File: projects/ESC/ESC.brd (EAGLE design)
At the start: 139.7 x 38.1 mm, 91 parts, among them J1 1755529, J2 1755529, J3 1755529, J4 1755529, U1 STM32F405RGT6, U10 CSD88584Q5DCT, U11 CSD88584Q5DCT, U12 CSD88584Q5DCT, U13 CSD88584Q5DCT, U2 CSD88584Q5DCT, U3 CSD88584Q5DCT, U4 CSD88584Q5DCT, U5 CSD88584Q5DCT, U6 CSD88584Q5DCT, U7 CSD88584Q5DCT, U8 CSD88584Q5DCT, U9 CSD88584Q5DCT, Y1 ECS-80-S-4X

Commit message: RIPUP MY LIFE
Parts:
- removed U$7: SAMTEC, VESC_SHIT:SAMTEC
- U$5: value SAMTEC -> ESC2BACKPLANE; device VESC_SHIT:SAMTEC -> ESC_to_Backplane_Connectors:ESC2BACKPLANE_WHOLE
- moved RED_LED 44.3 mm to (53.3, 6.10), turned to 90 degrees
- moved GREEN_LED 43.4 mm to (55.1, 6.10), turned to 90 degrees
- moved R2 40.1 mm to (53.3, 9.40), turned to 90 degrees
- moved R1 39.1 mm to (55.1, 9.40), turned to 90 degrees
- moved U3 38.9 mm to (21.6, 71.9)
- moved C13 38.9 mm to (43.9, 67.8)
- moved C14 38.9 mm to (38.1, 57.7)
- moved C17 38.9 mm to (41.9, 67.8)
- moved C22 38.9 mm to (35.4, 43.8)
- moved C23 38.9 mm to (33.7, 44.6)
- moved C24 38.9 mm to (43.9, 44.1)
- moved C25 38.9 mm to (44.1, 49.1)
- moved R10 38.9 mm to (43.7, 56.9)
- moved R11 38.9 mm to (46.0, 56.9)
- moved R18 38.9 mm to (30.1, 50.9)
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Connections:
- removed net 12V: U$5.P1-1, U$5.P1-2, U$5.P1-3, U$5.P1-4, U$5.P1-5, U$5.P1-6, U$5.P1-7, U$5.P1-8, U$5.P2-1, U$5.P2-2, U$5.P2-3, U$5.P2-4, U$5.P2-5, U$5.P2-6, U$5.P2-7, U$5.P2-8, U$5.P3-1, U$5.P3-2, U$5.P3-3, U$5.P3-4, U$5.P3-5, U$5.P3-6, U$5.P3-7, U$5.P3-8, U$5.P4-1, U$5.P4-2, U$5.P4-3, U$5.P4-4, U$5.P4-5, U$5.P4-6, U$5.P4-7, U$5.P4-8
- net +3V3: no longer U$5.1, U$5.10, U$5.11, U$5.12, U$5.13, U$5.14, U$5.15, U$5.16, U$5.17, U$5.18, U$5.19, U$5.2, U$5.20, U$5.21, U$5.22, U$5.23, U$5.24, U$5.3, U$5.4, U$5.5, U$5.6, U$5.7, U$5.8, U$5.9
- net CAN_H: no longer U$7.24
- net CAN_L: no longer U$7.23
- net GND: no longer U$7.P1-1, U$7.P1-2, U$7.P1-3, U$7.P1-4, U$7.P1-5, U$7.P1-6, U$7.P1-7, U$7.P1-8, U$7.P2-1, U$7.P2-2, U$7.P2-3, U$7.P2-4, U$7.P2-5, U$7.P2-6, U$7.P2-7, U$7.P2-8, U$7.P3-1, U$7.P3-2, U$7.P3-3, U$7.P3-4, U$7.P3-5, U$7.P3-6, U$7.P3-7, U$7.P3-8, U$7.P4-1, U$7.P4-2, U$7.P4-3, U$7.P4-4, U$7.P4-5, U$7.P4-6, U$7.P4-7, U$7.P4-8
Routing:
- net +3V3: track 144.9 -> 47.8 mm
- net VM_2: track 70.8 -> 0.00 mm, vias 6 -> 0
- net VM_1: track 64.5 -> 0.00 mm, vias 4 -> 0
- net NRST: track 85.5 -> 24.6 mm
- net INHC_3: track 69.9 -> 16.1 mm
- net INL_3: track 73.5 -> 21.0 mm
- net INHB_3: track 66.2 -> 18.3 mm
- net INHA_3: track 65.8 -> 18.9 mm
- net EN_3: track 60.1 -> 19.1 mm
- net FAULT_3: track 66.8 -> 25.9 mm
- net SWDIO: track 40.5 -> 1.78 mm
- net INHC_4: track 56.9 -> 20.0 mm
- net SLA_2: track 36.0 -> 0.00 mm
- net SWCLK: track 37.1 -> 1.87 mm
- net INL_4: track 59.1 -> 24.4 mm
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- removed copper zone on layer 1, net +3V3
- removed copper zone on layer 1, net 12V
- removed copper zone on layer 1, net 12V1

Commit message: Some changes have been made
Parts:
- moved U5 47.4 mm to (13.8, 10.4)
- moved U6 40.1 mm to (13.8, 4.06)
- moved U7 34.2 mm to (13.8, 17.0)

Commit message: making some changes
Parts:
- added C6: 0.1uF, SparkFun-Capacitors:0603
- added R6: 1.5k, SparkFun-Resistors:0603
- added U14: SN74CBTLV3257PWR, SN74CBTLV3257PWR:SN74CBTLV3257PWR
- moved U$5 44.1 mm to (53.3, 35.8), turned to 270 degrees
- moved GREEN_LED 3.84 mm to (58.9, 5.59)
- moved RED_LED 3.84 mm to (57.1, 5.59)
- moved R1 3.84 mm to (58.9, 8.89)
- moved R2 3.84 mm to (57.1, 8.89)
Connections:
- new net +12V: U$5.P$10, U$5.P$11, U$5.P$12, U$5.P$13, U$5.P$23, U$5.P$24, U$5.P$25, U$5.P$26, U$5.P$27, U$5.P$9, U$5.P$A, U$5.P$B, U$5.P$C, U$5.P$D, U$5.P$E, U$5.P$O, U$5.P$P, U$5.P$Q, U$5.P$R, U$5.P$S
- new net N$10: R6.1, U14.P$15
- new net NRST_IN: U14.P$9
- new net PROG_SEL: U$5.P$5
- new net S: U$6.S, U14.P$1
- new net SWCLK_IN: U14.P$4
- new net SWDIO_IN: U14.P$7
- net +3V3: now also C6.1, R6.2, U$5.P$G, U$5.P$H, U$5.P$U, U$5.P$V, U14.P$16
- net CAN_H: now also U$5.P$6
- net CAN_L: now also U$5.P$7
- net GND: now also C6.2, U$5.P$1, U$5.P$15, U$5.P$16, U$5.P$17, U$5.P$18, U$5.P$2, U$5.P$3, U$5.P$4, U$5.P$AA, U$5.P$BB, U$5.P$J, U$5.P$K, U$5.P$L, U$5.P$M, U$5.P$N, U$5.P$X, U$5.P$Y, U$5.P$Z, U14.P$8
- net NRST: now also U14.P$11
- net SWCLK: now also U14.P$2
- net SWDIO: now also U14.P$5
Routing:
- net FAULT_3: track 25.9 -> 2.42 mm, vias 1 -> 0
- net INL_4: track 24.4 -> 2.97 mm, vias 1 -> 0
- net GLC_3: track 21.1 -> 0.00 mm, vias 2 -> 0
- net SLC_3: track 24.1 -> 3.57 mm, vias 2 -> 0
- net NRST: track 24.6 -> 4.51 mm, vias 3 -> 1
- net EN_4: track 20.1 -> 0.03 mm
- net INL_3: track 21.0 -> 2.25 mm, vias 1 -> 0
- net INHC_4: track 20.0 -> 1.46 mm, vias 1 -> 0
- net VM_3: track 84.2 -> 66.3 mm, vias 2 -> 0
- net FAULT_4: track 17.8 -> 0.04 mm
- net SLB_3: track 20.0 -> 2.97 mm, vias 2 -> 1
- net INHB_4: track 19.4 -> 2.69 mm, vias 1 -> 0
- net EN_3: track 19.1 -> 2.50 mm, vias 1 -> 0
- net SHA_4: track 16.5 -> 0.54 mm
- net INHA_4: track 18.0 -> 2.23 mm, vias 1 -> 0
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- removed copper zone on layer 1, net VM_4

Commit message: REDESIGN preliminary 1
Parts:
- moved U3 43.7 mm to (13.5, 29.0)
- moved U4 40.2 mm to (23.1, 29.0), turned to 270 degrees
- moved U2 37.2 mm to (33.3, 29.0)
- moved C14 36.0 mm to (47.2, 22.9), flipped to the top, turned to 270 degrees
- moved C15 35.8 mm to (40.4, 35.6), turned to 180 degrees
- moved R7 35.8 mm to (41.5, 22.7), turned to 90 degrees
- moved C13 35.2 mm to (47.5, 32.8), turned to 0 degrees
- moved R8 34.2 mm to (42.6, 22.8), flipped to the bottom, turned to 180 degrees
- moved R11 34.2 mm to (48.8, 22.9), flipped to the bottom, turned to 0 degrees
- moved U$2 34.2 mm to (43.4, 28.7)
- moved R10 34.1 mm to (45.7, 22.9), flipped to the bottom, turned to 0 degrees
- moved R9 33.3 mm to (39.6, 22.9), turned to 180 degrees
- moved C17 32.4 mm to (44.7, 35.6), turned to 180 degrees
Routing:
- net SLA_1: track 0.00 -> 40.3 mm, vias 0 -> 2
- net GLA_1: track 0.00 -> 37.4 mm, vias 0 -> 2
- net SHA_1: track 0.00 -> 36.7 mm, vias 0 -> 2
- net GHA_1: track 0.00 -> 32.8 mm, vias 0 -> 2
- net PHASE_C1: track 0.00 -> 31.8 mm
- net SLB_1: track 0.00 -> 29.3 mm, vias 0 -> 2
- net SHB_1: track 0.00 -> 23.2 mm, vias 0 -> 2
- net PHASE_B1: track 0.00 -> 23.0 mm
- net GHB_1: track 0.00 -> 21.2 mm, vias 0 -> 2
- net GLB_1: track 0.00 -> 20.8 mm, vias 0 -> 2
- net PHASE_A1: track 0.00 -> 18.2 mm
- net SLC_1: track 0.00 -> 11.5 mm
- net SHC_1: track 0.00 -> 11.4 mm
- net N$19: track 0.00 -> 10.4 mm, vias 0 -> 1
- net GHC_1: track 0.00 -> 8.71 mm, vias 0 -> 2
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- added copper zone on layer 1, net VM_1

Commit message: some stuff
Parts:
- moved U$1 43.8 mm to (42.5, 6.96)
- moved U7 10.5 mm to (22.2, 10.7)
- moved U5 5.34 mm to (14.1, 15.7)
- moved U6 0.80 mm to (14.1, 4.83)

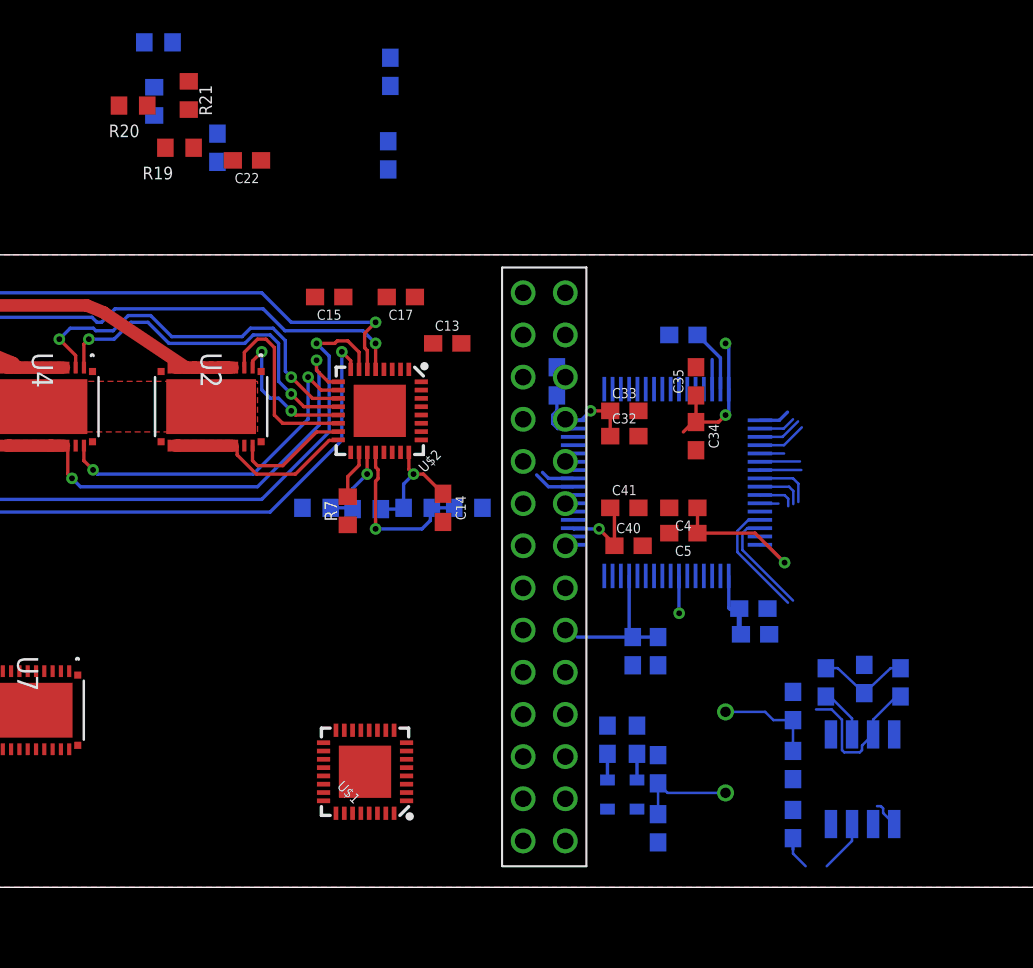
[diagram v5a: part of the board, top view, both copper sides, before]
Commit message: continued edits of drv setup
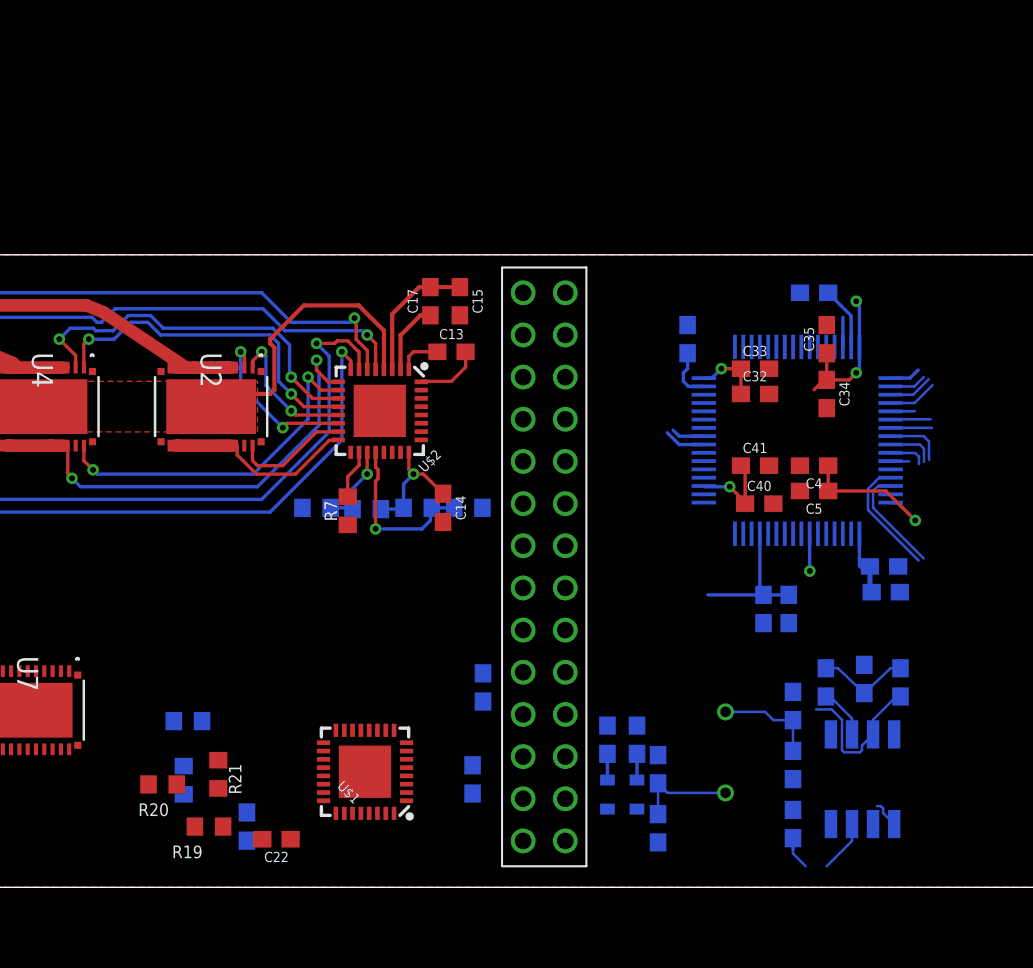
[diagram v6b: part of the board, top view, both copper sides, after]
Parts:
- moved R18 40.9 mm to (31.9, 10.0)
- moved C22 40.9 mm to (37.2, 2.90)
- moved C23 40.9 mm to (35.4, 3.66)
- moved R19 40.9 mm to (33.1, 3.66)
- moved R20 40.9 mm to (30.4, 6.20)
- moved R21 40.9 mm to (33.7, 6.81)
- moved R22 40.9 mm to (31.6, 6.45)
- moved C24 37.9 mm to (49.0, 6.50)
- moved C25 37.5 mm to (49.7, 12.0)
- moved C32 8.27 mm to (66.0, 29.7)
- moved C33 8.27 mm to (66.0, 31.2)
- moved C41 8.27 mm to (66.0, 25.4)
- moved C1 8.27 mm to (69.6, 35.8)
- moved C16 8.27 mm to (68.1, 16.8)
- moved C3 8.27 mm to (62.0, 33.0)
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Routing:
- net VM_1: track 0.00 -> 26.1 mm
- net N$34: track 0.00 -> 4.35 mm
- net N$16: track 0.00 -> 3.96 mm
- net N$9: track 0.00 -> 2.61 mm
- net SHC_1: track 11.4 -> 10.1 mm, vias 0 -> 2
- net SHA_1: track 36.7 -> 35.7 mm

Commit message: other edits
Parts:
- moved C6 83.5 mm to (80.5, 10.9), turned to 90 degrees
- moved R6 81.6 mm to (80.5, 14.2), turned to 90 degrees
- moved U14 68.9 mm to (67.6, 15.0)
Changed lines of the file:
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@@
 <attribute name="VALUE" x="68.64743125" y="13.90911875" size="1.27245" layer="28" rot="MR270"/>
 </element>
-<element name="U14" library="SN74CBTLV3257PWR" package="SN74CBTLV3257PWR" value="SN74CBTLV3257PWR" x="1.016" y="-3.048" smashed="yes">
-<attribute name="NAME" x="2.286" y="-14.478" size="1.016" layer="25" ratio="7"/>
-<attribute name="VALUE" x="2.286" y="-1.778" size="1.016" layer="25" ratio="7"/>
+<element name="U14" library="SN74CBTLV3257PWR" package="SN74CBTLV3257PWR" value="SN74CBTLV3257PWR" x="67.564" y="14.986" smashed="yes">
+<attribute name="NAME" x="68.834" y="3.556" size="1.016" layer="25" ratio="7"/>
+<attribute name="VALUE" x="68.834" y="16.256" size="1.016" layer="25" ratio="7"/>
 </element>
-<element name="C6" library="SparkFun-Capacitors" library_urn="urn:adsk.eagle:library:510" package="0603" package3d_urn="urn:adsk.eagle:package:37414/1" value="0.1uF" x="1.778" y="-16.764" smashed="yes">
-<attribute name="NAME" x="1.778" y="-16.002" size="0.6096" layer="25" font="vector" ratio="20" align="bottom-center"/>
-<attribute name="PROD_ID" value="CAP-00810" x="-6.604" y="-1.778" size="1.778" layer="27" display="off"/>
-<attribute name="VALUE" x="1.778" y="-17.526" size="0.6096" layer="27" font="vector" ratio="20" align="top-center"/>
+<element name="C6" library="SparkFun-Capacitors" library_urn="urn:adsk.eagle:library:510" package="0603" package3d_urn="urn:adsk.eagle:package:37414/1" value="0.1uF" x="80.518" y="10.922" smashed="yes" rot="R90">
+<attribute name="NAME" x="79.756" y="10.922" size="0.6096" layer="25" font="vector" ratio="20" rot="R90" align="bottom-center"/>
+<attribute name="PROD_ID" value="CAP-00810" x="65.532" y="2.54" size="1.778" layer="27" rot="R90" display="off"/>
+<attribute name="VALUE" x="81.28" y="10.922" size="0.6096" layer="27" font="vector" ratio="20" rot="R90" align="top-center"/>
 </element>
-<element name="R6" library="SparkFun-Resistors" library_urn="urn:adsk.eagle:library:532" package="0603" package3d_urn="urn:adsk.eagle:package:39650/1" value="1.5k" x="5.08" y="-16.764" smashed="yes">
-<attribute name="NAME" x="5.08" y="-16.002" size="0.6096" layer="25" font="vector" ratio="20" align="bottom-center"/>
-<attribute name="PROD_ID" value="RES-08306" x="-6.604" y="-5.08" size="1.778" layer="27" display="off"/>
-<attribute name="VALUE" x="5.08" y="-17.526" size="0.6096" layer="27" font="vector" ratio="20" align="top-center"/>
+<element name="R6" library="SparkFun-Resistors" library_urn="urn:adsk.eagle:library:532" package="0603" package3d_urn="urn:adsk.eagle:package:39650/1" value="1.5k" x="80.518" y="14.224" smashed="yes" rot="R90">
+<attribute name="NAME" x="79.756" y="14.224" size="0.6096" layer="25" font="vector" ratio="20" rot="R90" align="bottom-center"/>
+<attribute name="PROD_ID" value="RES-08306" x="68.834" y="2.54" size="1.778" layer="27" rot="R90" display="off"/>
+<attribute name="VALUE" x="81.28" y="14.224" size="0.6096" layer="27" font="vector" ratio="20" rot="R90" align="top-center"/>
 </element>
 <element name="U$5" library="ESC_to_Backplane_Connectors" package="ESC2BACKPLANE_WHOLE" value="ESC2BACKPLANE" x="53.34" y="35.814" smashed="yes" rot="R270"/>
@@
 <wire x1="68.746" y1="35.814" x2="70.358" y2="33.87" width="0" layer="19" extent="1-16"/>
 <wire x1="61.976" y1="33.87" x2="66.89" y2="31.242" width="0" layer="19" extent="1-16"/>
-<wire x1="68.326" y1="4.66" x2="68.326" y2="11.772" width="0" layer="19" extent="16-16"/>
+<wire x1="67.564" y1="6.096" x2="68.326" y2="11.772" width="0" layer="19" extent="1-16"/>
+<wire x1="68.326" y1="4.66" x2="67.564" y2="6.096" width="0" layer="19" extent="1-16"/>
 <wire x1="73.152" y1="3.81" x2="68.326" y2="4.66" width="0" layer="19" extent="16-16"/>
-<wire x1="60.198" y1="7.962" x2="68.326" y2="4.66" width="0" layer="19" extent="16-16"/>
+<wire x1="60.198" y1="7.962" x2="67.564" y2="6.096" width="0" layer="19" extent="1-16"/>
 <wire x1="58.928" y1="4.7117" x2="60.198" y2="7.962" width="0" layer="19" extent="16-16"/>
 <wire x1="57.15" y1="4.7117" x2="58.928" y2="4.7117" width="0" layer="19" extent="16-16"/>
@@
 <wire x1="29.503" y1="6.1976" x2="31.623" y2="5.6016" width="0" layer="19" extent="1-16"/>
 <wire x1="31.027" y1="10.0076" x2="29.503" y2="6.1976" width="0" layer="19" extent="1-16"/>
+<wire x1="80.518" y1="11.772" x2="72.6186" y2="13.3976" width="0" layer="19" extent="1-16"/>
 <wire x1="49.618" y1="22.86" x2="52.07" y2="12.954" width="0" layer="19" extent="16-16"/>
 <wire x1="47.244" y1="22.01" x2="49.618" y2="22.86" width="0" layer="19" extent="1-16"/>
@@
 <wire x1="41.5036" y1="21.8322" x2="44.684" y2="26.202" width="0" layer="19" extent="1-1"/>
 <wire x1="38.774" y1="22.86" x2="41.5036" y2="21.8322" width="0" layer="19" extent="1-16"/>
-<wire x1="1.016" y1="-11.938" x2="29.503" y2="6.1976" width="0" layer="19" extent="1-1"/>
-<wire x1="2.628" y1="-16.764" x2="1.016" y2="-11.938" width="0" layer="19" extent="1-1"/>
 </signal>
 <signal name="+3V3">
@@
 <contactref element="U$5" pad="P$V"/>
 <contactref element="U$5" pad="P$U"/>
-<wire x1="75.692" y1="22.098" x2="89.662" y2="24.892" width="0" layer="19" extent="1-1"/>
-<wire x1="72.33" y1="21.2979" x2="74.2061" y2="23.174" width="0" layer="19" extent="16-16"/>
+<wire x1="80.518" y1="15.074" x2="89.662" y2="24.892" width="0" layer="19" extent="1-1"/>
+<wire x1="80.518" y1="10.072" x2="80.518" y2="15.074" width="0" layer="19" extent="1-1"/>
+<wire x1="72.964" y1="14.986" x2="80.518" y2="15.074" width="0" layer="19" extent="1-1"/>
+<wire x1="73.064" y1="17.78" x2="72.964" y2="14.986" width="0" layer="19" extent="1-16"/>
+<wire x1="74.2061" y1="23.174" x2="72.33" y2="21.2979" width="0" layer="19" extent="16-16"/>
 <wire x1="69.596" y1="29.972" x2="70.446" y2="25.4" width="0" layer="19" extent="1-1"/>
 <wire x1="65.19" y1="29.718" x2="69.596" y2="29.972" width="0" layer="19" extent="1-1"/>
@@
 <wire x1="52.07" y1="20.574" x2="54.61" y2="20.574" width="0" layer="19" extent="1-1"/>
 <wire x1="52.07" y1="18.034" x2="54.61" y2="18.034" width="0" layer="19" extent="1-1"/>
-<wire x1="71.882" y1="3.81" x2="73.064" y2="17.78" width="0" layer="19" extent="16-16"/>
+<wire x1="71.882" y1="3.81" x2="80.518" y2="10.072" width="0" layer="19" extent="1-16"/>
 <wire x1="69.088" y1="1.27" x2="70.358" y2="1.27" width="0" layer="19" extent="16-16"/>
 <wire x1="99.822" y1="12.026" x2="89.662" y2="24.892" width="0" layer="19" extent="16-16"/>
-<wire x1="6.416" y1="-3.048" x2="52.07" y2="18.034" width="0" layer="19" extent="1-1"/>
-<wire x1="5.93" y1="-16.764" x2="6.416" y2="-3.048" width="0" layer="19" extent="1-1"/>
-<wire x1="0.928" y1="-16.764" x2="5.93" y2="-16.764" width="0" layer="19" extent="1-1"/>
 </signal>
 <signal name="NRST">
@@
 <wire x1="99.822" y1="10.326" x2="89.662" y2="35.052" width="0" layer="19" extent="16-16"/>
 <wire x1="101.854" y1="10.326" x2="99.822" y2="10.326" width="0" layer="19" extent="16-16"/>
-<wire x1="6.416" y1="-9.398" x2="69.342" y2="19.05" width="0" layer="19" extent="1-1"/>
+<wire x1="72.964" y1="8.636" x2="69.342" y2="19.05" width="0" layer="19" extent="1-1"/>
 </signal>
 <signal name="SWDIO">
@@
 <contactref element="U14" pad="P$5"/>
 <wire x1="71.33" y1="32.5501" x2="89.662" y2="32.512" width="0" layer="19" extent="16-16"/>
-<wire x1="1.016" y1="-8.128" x2="71.33" y2="32.5501" width="0" layer="19" extent="1-16"/>
+<wire x1="67.564" y1="9.906" x2="71.33" y2="32.5501" width="0" layer="19" extent="1-16"/>
 </signal>
 <signal name="SWCLK">
@@
 <contactref element="U14" pad="P$2"/>
 <wire x1="75.8698" y1="31.1658" x2="89.662" y2="27.432" width="0" layer="19" extent="16-16"/>
-<wire x1="1.016" y1="-4.318" x2="74.2061" y2="30.674" width="0" layer="19" extent="1-16"/>
+<wire x1="67.564" y1="13.716" x2="74.2061" y2="30.674" width="0" layer="19" extent="1-16"/>
 </signal>
 <signal name="PHASE_A1">
@@
 <contactref element="U14" pad="P$1"/>
 <contactref element="U$6" pad="S"/>
-<wire x1="1.016" y1="-3.048" x2="74.422" y2="9.21" width="0" layer="19" extent="1-16"/>
+<wire x1="67.564" y1="14.986" x2="74.422" y2="9.21" width="0" layer="19" extent="1-16"/>
 </signal>
 <signal name="N$10">
 <contactref element="U14" pad="P$15"/>
 <contactref element="R6" pad="1"/>
-<wire x1="6.416" y1="-4.318" x2="4.23" y2="-16.764" width="0" layer="19" extent="1-1"/>
+<wire x1="72.964" y1="13.716" x2="80.518" y2="13.374" width="0" layer="19" extent="1-1"/>
 </signal>
 <signal name="SWCLK_IN">
